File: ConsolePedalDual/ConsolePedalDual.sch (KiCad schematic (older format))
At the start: 14 parts, among them J1 AudioJack3, J2 AudioJack2, J3 Conn_02x25_Odd_Even, J4 Conn_02x25_Odd_Even, SW1 Bypass

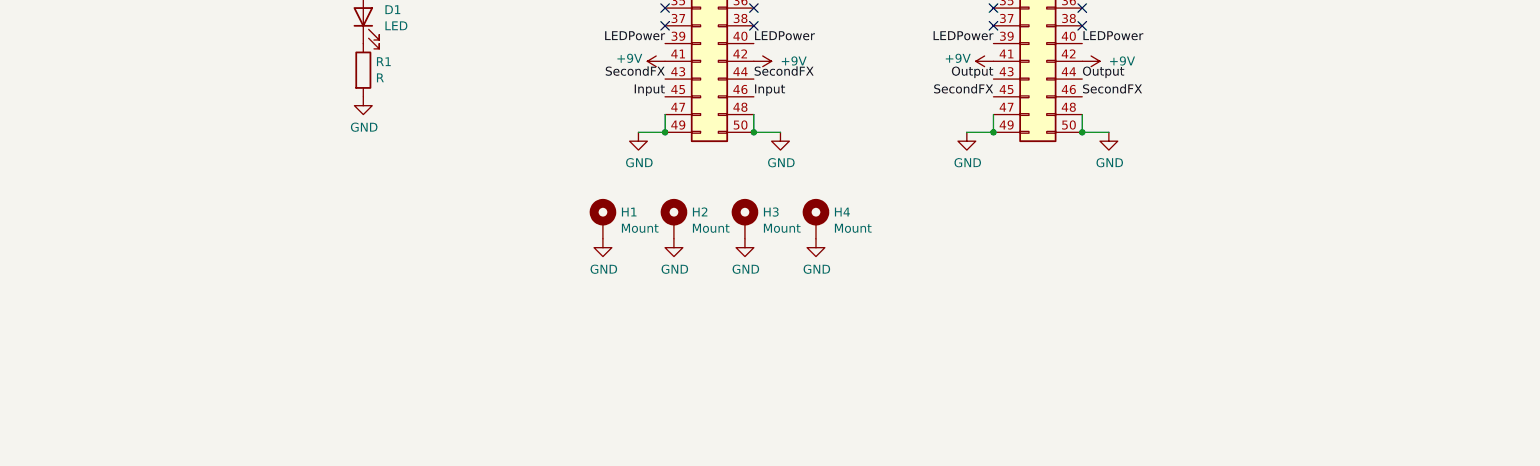
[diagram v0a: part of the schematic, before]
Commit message: Trying to visualize how audio switching ic is going to work
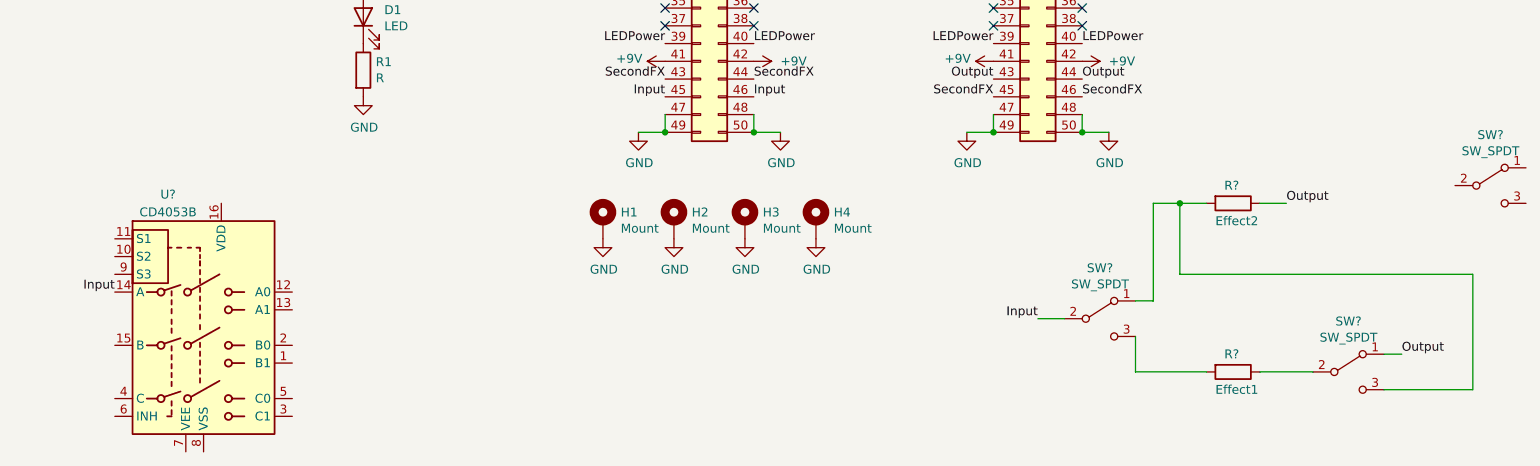
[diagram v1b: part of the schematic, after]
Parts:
- added R?: Effect1, Resistor_THT:R_Axial_DIN0207_L6.3mm_D2.5mm_P10.16mm_Horizontal, symbol Device:R
- added R?: Effect2, Resistor_THT:R_Axial_DIN0207_L6.3mm_D2.5mm_P10.16mm_Horizontal, symbol Device:R
- added SW? (x3): SW_SPDT, symbol Switch:SW_SPDT
- added U?: CD4053B, symbol Analog_Switch:CD4053B
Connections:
- net Input: now also SW?.2 (B), U?.14 (A)
- net Output: now also R?.1, SW?.1 (A)
- new net: R?.2, SW?.1 (A), SW?.3 (C)
- new net: R?.2, SW?.3 (C)
- new net: R?.1, SW?.2 (B)
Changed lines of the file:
@@
 	1    0    0    -1
 $EndComp
+$Comp
+L Analog_Switch:CD4053B U?
+U 1 1 60FF6D67
+P 3200 5700
+F 0 "U?" H 3000 6450 50  0000 C CNN
+F 1 "CD4053B" H 3000 6350 50  0000 C CNN
+F 2 "" H 3350 4950 50  0001 L CNN
+F 3 "http://www.ti.com/lit/ds/symlink/cd4052b.pdf" H 3180 5900 50  0001 C CNN
+	1    3200 5700
+	1    0    0    -1
+$EndComp
+$Comp
+L Switch:SW_SPDT SW?
+U 1 1 60FFC9EC
+P 8250 5650
+F 0 "SW?" H 8250 5935 50  0000 C CNN
+F 1 "SW_SPDT" H 8250 5844 50  0000 C CNN
+F 2 "" H 8250 5650 50  0001 C CNN
+F 3 "~" H 8250 5650 50  0001 C CNN
+	1    8250 5650
+	1    0    0    -1
+$EndComp
+$Comp
+L Switch:SW_SPDT SW?
+U 1 1 60FFD888
+P 10450 4900
+F 0 "SW?" H 10450 5185 50  0000 C CNN
+F 1 "SW_SPDT" H 10450 5094 50  0000 C CNN
+F 2 "" H 10450 4900 50  0001 C CNN
+F 3 "~" H 10450 4900 50  0001 C CNN
+	1    10450 4900
+	1    0    0    -1
+$EndComp
+$Comp
+L Switch:SW_SPDT SW?
+U 1 1 60FFDC32
+P 9650 5950
+F 0 "SW?" H 9650 6235 50  0000 C CNN
+F 1 "SW_SPDT" H 9650 6144 50  0000 C CNN
+F 2 "" H 9650 5950 50  0001 C CNN
+F 3 "~" H 9650 5950 50  0001 C CNN
+	1    9650 5950
+	1    0    0    -1
+$EndComp
+Text Label 7900 5650 2    50   ~ 0
+Input
+Wire Wire Line
+	7900 5650 8050 5650
+Text Label 9950 5850 0    50   ~ 0
+Output
+Wire Wire Line
+	9950 5850 9850 5850
+$Comp
+L Device:R R?
+U 1 1 61005F42
+P 9000 5950
+F 0 "R?" V 8900 5900 50  0000 L CNN
+F 1 "Effect1" V 9100 5850 50  0000 L CNN
+F 2 "Resistor_THT:R_Axial_DIN0207_L6.3mm_D2.5mm_P10.16mm_Horizontal" V 8930 5950 50  0001 C CNN
+F 3 "~" H 9000 5950 50  0001 C CNN
+	1    9000 5950
+	0    1    1    0
+$EndComp
+Wire Wire Line
+	8450 5750 8450 5950
+Wire Wire Line
+	8450 5950 8850 5950
+Wire Wire Line
+	9150 5950 9450 5950
+$Comp
+L Device:R R?
+U 1 1 6100AEB1
+P 9000 5000
+F 0 "R?" V 8900 4950 50  0000 L CNN
+F 1 "Effect2" V 9100 4900 50  0000 L CNN
+F 2 "Resistor_THT:R_Axial_DIN0207_L6.3mm_D2.5mm_P10.16mm_Horizontal" V 8930 5000 50  0001 C CNN
+F 3 "~" H 9000 5000 50  0001 C CNN
+	1    9000 5000
+	0    1    1    0
+$EndComp
+Wire Wire Line
+	8450 5550 8550 5550
+Wire Wire Line
+	8550 5550 8550 5000
+Wire Wire Line
+	8550 5000 8700 5000
+Text Label 9300 5000 0    50   ~ 0
+Output
+Wire Wire Line
+	9300 5000 9150 5000
+Wire Wire Line
+	9850 6050 10350 6050
+Wire Wire Line
+	10350 6050 10350 5400
+Wire Wire Line
+	10350 5400 8700 5400
+Wire Wire Line
+	8700 5400 8700 5000
+Connection ~ 8700 5000
+Wire Wire Line
+	8700 5000 8850 5000
+Text Label 2700 5500 2    50   ~ 0
+Input
 $EndSCHEMATC

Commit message: Minor changes
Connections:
- net +9V: now also U?.16 (VDD)
- net GND: now also U?.6 (INH), U?.7 (VEE), U?.8 (VSS)
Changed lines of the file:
@@
 Text Label 2700 5500 2    50   ~ 0
 Input
+$Comp
+L power:+9V #PWR?
+U 1 1 61013CBC
+P 3300 5000
+F 0 "#PWR?" H 3300 4850 50  0001 C CNN
+F 1 "+9V" H 3200 5150 50  0000 L CNN
+F 2 "" H 3300 5000 50  0001 C CNN
+F 3 "" H 3300 5000 50  0001 C CNN
+	1    3300 5000
+	1    0    0    -1
+$EndComp
+$Comp
+L power:GND #PWR?
+U 1 1 61016125
+P 3100 6450
+F 0 "#PWR?" H 3100 6200 50  0001 C CNN
+F 1 "GND" H 3105 6277 50  0000 C CNN
+F 2 "" H 3100 6450 50  0001 C CNN
+F 3 "" H 3100 6450 50  0001 C CNN
+	1    3100 6450
+	1    0    0    -1
+$EndComp
+Wire Wire Line
+	3200 6400 3100 6400
+Wire Wire Line
+	3100 6400 3100 6450
+Connection ~ 3100 6400
+Wire Wire Line
+	3100 6400 2700 6400
+Wire Wire Line
+	2700 6400 2700 6200
 $EndSCHEMATC

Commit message: Finished schematic. Trying to figure out how to fit all these components on this board
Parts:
- removed R?: Effect1, Resistor_THT:R_Axial_DIN0207_L6.3mm_D2.5mm_P10.16mm_Horizontal, symbol Device:R
- removed R?: Effect2, Resistor_THT:R_Axial_DIN0207_L6.3mm_D2.5mm_P10.16mm_Horizontal, symbol Device:R
- removed SW1: Bypass, Connector_PinSocket_2.54mm:PinSocket_1x02_P2.54mm_Vertical, symbol Switch:SW_SPST
- removed SW? (x3): SW_SPDT, symbol Switch:SW_SPDT
- added C1: 47uF, Capacitor_THT:CP_Radial_D6.3mm_P2.50mm, symbol Device:CP
- added C2, C3, C4, C5, C6, C7: 2.2uF, Capacitor_THT:CP_Radial_D4.0mm_P2.00mm, symbol Device:CP
- added R2, R3: 10K, Resistor_THT:R_Axial_DIN0207_L6.3mm_D2.5mm_P10.16mm_Horizontal, symbol Device:R
- added R4, R5, R6, R7, R8, R9: 510K, Resistor_THT:R_Axial_DIN0207_L6.3mm_D2.5mm_P10.16mm_Horizontal, symbol Device:R
- J3: value Conn_02x25_Odd_Even -> Slot A
- J4: value Conn_02x25_Odd_Even -> Slot B
- R1: value R -> LED
- U1: renamed from U?; footprint (none) -> Package_DIP:DIP-16_W7.62mm_Socket
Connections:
- net +9V: now also R2.1; no longer J3.10 (Pin_10), J3.42 (Pin_42), J4.10 (Pin_10), J4.42 (Pin_42)
- net GND: now also U1.9 (S3), C1.2, R3.2
- net Input: now also C2.2; no longer J3.45 (Pin_45), J3.46 (Pin_46), J3.5 (Pin_5), J3.6 (Pin_6), U1.14 (A)
- net Output: now also C6.2
- net at U1.1 (B1): now also C7.1, R9.1
- net SlotB: now reaches U1.10 (S2)
- net SlotB: now also J4.10 (Pin_10), J4.42 (Pin_42)
- net SlotA: now reaches U1.11 (S1)
- net SlotA: now also J3.10 (Pin_10), J3.42 (Pin_42)
- net at U1.12 (A0): now also C4.1, R6.2
- net at U1.13 (A1): now also C5.1, R7.1
- net at U1.15 (B): now also C3.1, R5.1
- net at U1.2 (B0): now also C6.1, R8.2
- net SecondFX renamed SlotAOutput
- net SlotAOutput: now also C3.2; no longer J4.45 (Pin_45), J4.46 (Pin_46), J4.5 (Pin_5), J4.6 (Pin_6)
- new net: C2.1, R4.1, U1.14 (A)
- new net SlotAInput: C5.2, J3.45 (Pin_45), J3.46 (Pin_46), J3.5 (Pin_5), J3.6 (Pin_6)
- new net SlotBInput: C4.2, C7.2, J4.45 (Pin_45), J4.46 (Pin_46), J4.5 (Pin_5), J4.6 (Pin_6)
- new net VREF: C1.1, R2.2, R3.1, R4.2, R5.2, R6.1, R7.2, R8.1, R9.2
- no-connect marks 53 -> 56
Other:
- moved on the sheet: BT1, D1, D2, H1, H2, H3, H4, J1, J2, J3, J4, R1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

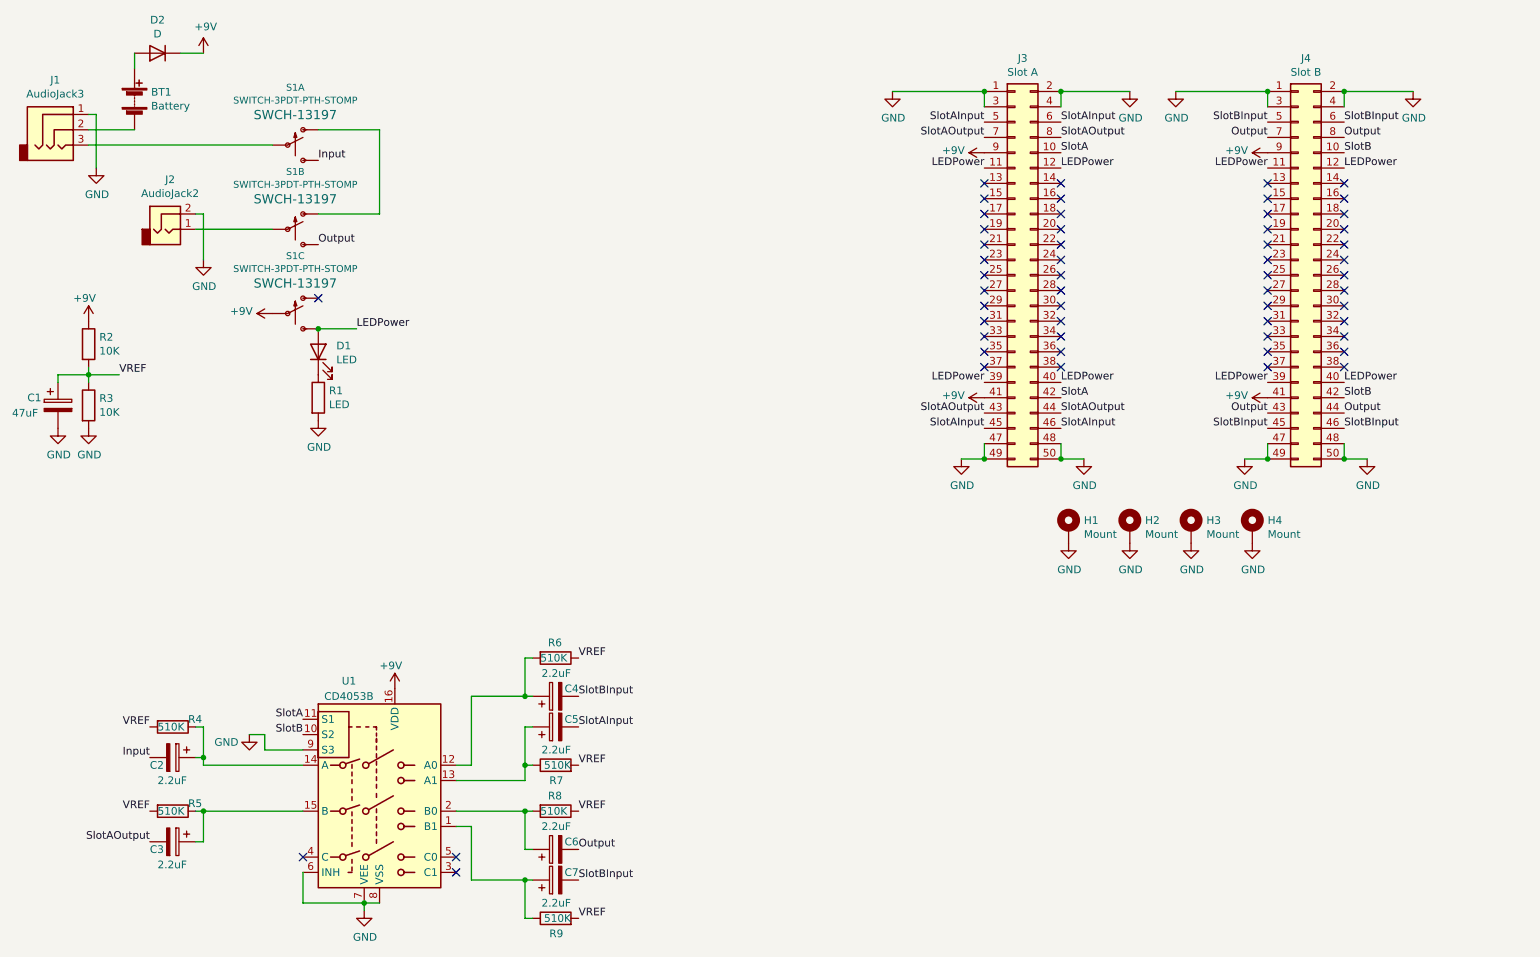
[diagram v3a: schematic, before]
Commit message: Added pull down resistors, fixed mounting hole placements, and fixed 3PDT switch footprint
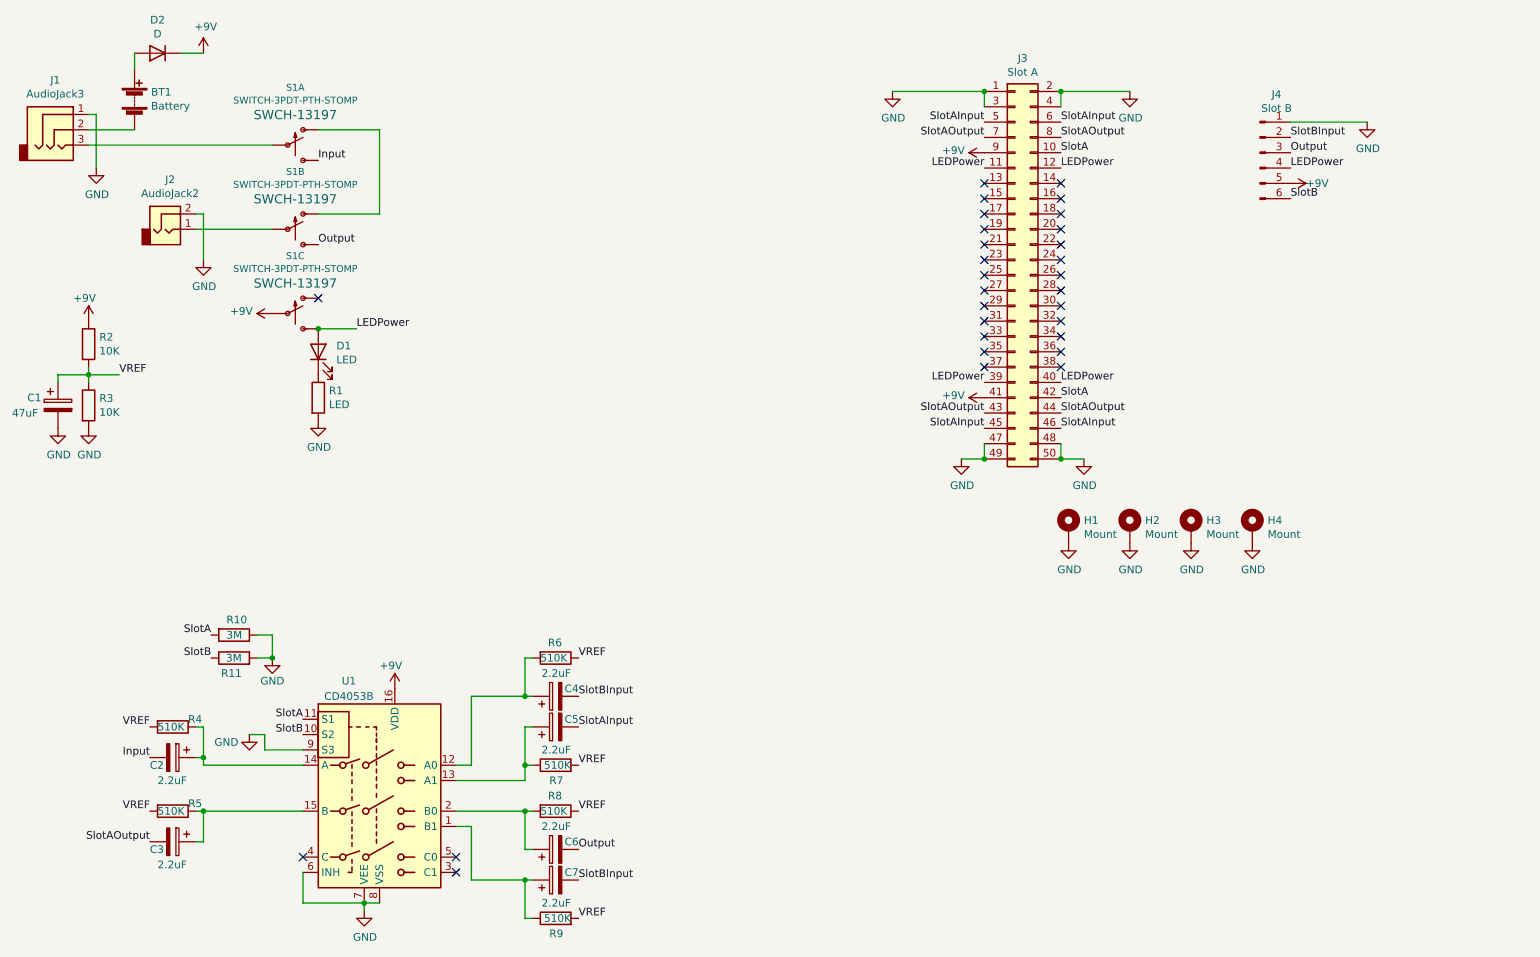
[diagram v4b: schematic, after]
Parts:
- removed J4: Slot B, libraries:n64Socket, symbol Connector_Generic:Conn_02x25_Odd_Even
- added J4: Slot B, Connector_PinSocket_2.54mm:PinSocket_1x06_P2.54mm_Vertical, symbol Connector:Conn_01x06_Male
- added R10, R11: 3M, Resistor_THT:R_Axial_DIN0207_L6.3mm_D2.5mm_P10.16mm_Horizontal, symbol Device:R
- S1: footprint MuffPi:STOMP_SWITCH_3PDT -> libraries:STOMP_SWITCH_3PDT
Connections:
- net +9V: now also J4.5 (Pin_5)
- net GND: now also J4.1 (Pin_1), R10.1, R11.2
- net LEDPower: now also J4.4 (Pin_4)
- net Output: now also J4.3 (Pin_3)
- net SlotA: now also R10.2
- net SlotB: now also J4.6 (Pin_6), R11.1
- net SlotBInput: now also J4.2 (Pin_2)
- no-connect marks 56 -> 30
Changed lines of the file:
@@
 F 0 "S1" H 2600 1976 45  0000 C CNN
 F 1 "SWITCH-3PDT-PTH-STOMP" H 2600 1892 45  0000 C CNN
-F 2 "MuffPi:STOMP_SWITCH_3PDT" H 2650 1850 20  0001 C CNN
+F 2 "libraries:STOMP_SWITCH_3PDT" H 2650 1850 20  0001 C CNN
 F 3 "" H 2650 1600 50  0001 C CNN
 F 4 "SWCH-13197" H 2600 1797 60  0000 C CNN "Field4"
@@
 F 0 "S1" H 2600 2526 45  0000 C CNN
 F 1 "SWITCH-3PDT-PTH-STOMP" H 2600 2442 45  0000 C CNN
-F 2 "MuffPi:STOMP_SWITCH_3PDT" H 2650 2400 20  0001 C CNN
+F 2 "libraries:STOMP_SWITCH_3PDT" H 2650 2400 20  0001 C CNN
 F 3 "" H 2650 2150 50  0001 C CNN
 F 4 "SWCH-13197" H 2600 2347 60  0000 C CNN "Field4"
@@
 F 0 "S1" H 2600 3076 45  0000 C CNN
 F 1 "SWITCH-3PDT-PTH-STOMP" H 2600 2992 45  0000 C CNN
-F 2 "MuffPi:STOMP_SWITCH_3PDT" H 2650 2950 20  0001 C CNN
+F 2 "libraries:STOMP_SWITCH_3PDT" H 2650 2950 20  0001 C CNN
 F 3 "" H 2650 2700 50  0001 C CNN
 F 4 "SWCH-13197" H 2600 2897 60  0000 C CNN "Field4"
@@
 Wire Wire Line
 	2000 1000 1850 1000
-Wire Wire Line
-	8950 1250 8950 1350
-$Comp
-L power:GND #PWR010
-U 1 1 60B0323C
-P 8350 1250
-F 0 "#PWR010" H 8350 1000 50  0001 C CNN
-F 1 "GND" H 8355 1077 50  0000 C CNN
-F 2 "" H 8350 1250 50  0001 C CNN
-F 3 "" H 8350 1250 50  0001 C CNN
-	1    8350 1250
-	1    0    0    -1
-$EndComp
-Wire Wire Line
-	8350 1250 8950 1250
-$Comp
-L power:+9V #PWR012
-U 1 1 60B03245
-P 8950 1650
-F 0 "#PWR012" H 8950 1500 50  0001 C CNN
-F 1 "+9V" V 8965 1778 50  0000 L CNN
-F 2 "" H 8950 1650 50  0001 C CNN
-F 3 "" H 8950 1650 50  0001 C CNN
-	1    8950 1650
-	0    -1   -1   0
-$EndComp
-Text Label 8950 1750 2    50   ~ 0
-LEDPower
-Text Label 9450 3150 0    50   ~ 0
-LEDPower
-Wire Wire Line
-	9450 3550 9450 3650
-Wire Wire Line
-	9450 3650 9600 3650
-$Comp
-L power:GND #PWR016
-U 1 1 60B03257
-P 9600 3650
-F 0 "#PWR016" H 9600 3400 50  0001 C CNN
-F 1 "GND" H 9605 3477 50  0000 C CNN
-F 2 "" H 9600 3650 50  0001 C CNN
-F 3 "" H 9600 3650 50  0001 C CNN
-	1    9600 3650
-	1    0    0    -1
-$EndComp
-$Comp
-L Connector_Generic:Conn_02x25_Odd_Even J4
-U 1 1 60B0325D
-P 9150 2450
-F 0 "J4" H 9200 3867 50  0000 C CNN
-F 1 "Slot B" H 9200 3776 50  0000 C CNN
-F 2 "libraries:n64Socket" H 9150 2450 50  0001 C CNN
-F 3 "~" H 9150 2450 50  0001 C CNN
-	1    9150 2450
-	1    0    0    -1
-$EndComp
-Connection ~ 8950 1250
-Connection ~ 9450 3650
-Wire Wire Line
-	9450 1350 9450 1250
-$Comp
-L power:GND #PWR017
-U 1 1 60B03266
-P 9900 1250
-F 0 "#PWR017" H 9900 1000 50  0001 C CNN
-F 1 "GND" H 9905 1077 50  0000 C CNN
-F 2 "" H 9900 1250 50  0001 C CNN
-F 3 "" H 9900 1250 50  0001 C CNN
-	1    9900 1250
-	1    0    0    -1
-$EndComp
-Wire Wire Line
-	9450 1250 9900 1250
-Connection ~ 9450 1250
-Text Label 9450 1750 0    50   ~ 0
-LEDPower
-Text Label 8950 3150 2    50   ~ 0
-LEDPower
-$Comp
-L power:+9V #PWR013
-U 1 1 60B03278
-P 8950 3250
-F 0 "#PWR013" H 8950 3100 50  0001 C CNN
-F 1 "+9V" V 8965 3378 50  0000 L CNN
-F 2 "" H 8950 3250 50  0001 C CNN
-F 3 "" H 8950 3250 50  0001 C CNN
-	1    8950 3250
-	0    -1   -1   0
-$EndComp
-Wire Wire Line
-	8950 3550 8950 3650
-$Comp
-L power:GND #PWR011
-U 1 1 60B03281
-P 8800 3650
-F 0 "#PWR011" H 8800 3400 50  0001 C CNN
-F 1 "GND" H 8805 3477 50  0000 C CNN
-F 2 "" H 8800 3650 50  0001 C CNN
-F 3 "" H 8800 3650 50  0001 C CNN
-	1    8800 3650
-	1    0    0    -1
-$EndComp
-Wire Wire Line
-	8800 3650 8950 3650
-Connection ~ 8950 3650
-NoConn ~ 9450 1850
-NoConn ~ 9450 1950
-NoConn ~ 9450 2050
-NoConn ~ 9450 2150
-NoConn ~ 9450 2250
-NoConn ~ 9450 2350
-NoConn ~ 9450 2450
-NoConn ~ 9450 2550
-NoConn ~ 9450 2650
-NoConn ~ 9450 2750
-NoConn ~ 9450 2850
-NoConn ~ 9450 2950
-NoConn ~ 9450 3050
-NoConn ~ 8950 3050
-NoConn ~ 8950 2950
-NoConn ~ 8950 2850
-NoConn ~ 8950 2750
-NoConn ~ 8950 2650
-NoConn ~ 8950 2550
-NoConn ~ 8950 2450
-NoConn ~ 8950 2350
-NoConn ~ 8950 2250
-NoConn ~ 8950 2150
-NoConn ~ 8950 2050
-NoConn ~ 8950 1950
-NoConn ~ 8950 1850
 $Comp
 L Mechanical:MountingHole_Pad H1
@@
 Text Label 7600 1650 0    50   ~ 0
 SlotA
-Text Label 9450 1650 0    50   ~ 0
-SlotB
 Text Label 7600 3250 0    50   ~ 0
 SlotA
-Text Label 9450 3250 0    50   ~ 0
-SlotB
 Text Label 7600 1450 0    50   ~ 0
 SlotAInput
@@
 Text Label 7600 3350 0    50   ~ 0
 SlotAOutput
-Text Label 8950 1450 2    50   ~ 0
-SlotBInput
-Text Label 9450 1450 0    50   ~ 0
-SlotBInput
-Text Label 8950 3450 2    50   ~ 0
-SlotBInput
-Text Label 9450 3450 0    50   ~ 0
-SlotBInput
 Text Label 4450 6200 0    50   ~ 0
 Output
 Text Label 4450 5400 0    50   ~ 0
 SlotAInput
-Text Label 9450 3350 0    50   ~ 0
-Output
-Text Label 8950 3350 2    50   ~ 0
-Output
-Text Label 9450 1550 0    50   ~ 0
-Output
-Text Label 8950 1550 2    50   ~ 0
-Output
 NoConn ~ 2650 6250
 $Comp
@@
 	3750 5200 4100 5200
 Connection ~ 4100 5200
+Text Label 2050 4800 2    50   ~ 0
+SlotA
+Text Label 2050 4950 2    50   ~ 0
+SlotB
+$Comp
+L Device:R R10
+U 1 1 61456261
+P 2200 4800
+F 0 "R10" V 2100 4750 50  0000 L CNN
+F 1 "3M" V 2200 4750 50  0000 L CNN
+F 2 "Resistor_THT:R_Axial_DIN0207_L6.3mm_D2.5mm_P10.16mm_Horizontal" V 2130 4800 50  0001 C CNN
+F 3 "~" H 2200 4800 50  0001 C CNN
+	1    2200 4800
+	0    1    1    0
+$EndComp
+$Comp
+L power:GND #PWR025
+U 1 1 61457C6D
+P 2450 4950
+F 0 "#PWR025" H 2450 4700 50  0001 C CNN
+F 1 "GND" H 2450 4800 50  0000 C CNN
+F 2 "" H 2450 4950 50  0001 C CNN
+F 3 "" H 2450 4950 50  0001 C CNN
+	1    2450 4950
+	1    0    0    -1
+$EndComp
+Wire Wire Line
+	2450 4800 2350 4800
+Wire Wire Line
+	2350 4950 2450 4950
+Wire Wire Line
+	2450 4800 2450 4950
+Connection ~ 2450 4950
+$Comp
+L Device:R R11
+U 1 1 61456971
+P 2200 4950
+F 0 "R11" V 2100 4900 50  0000 L CNN
+F 1 "3M" V 2200 4900 50  0000 L CNN
+F 2 "Resistor_THT:R_Axial_DIN0207_L6.3mm_D2.5mm_P10.16mm_Horizontal" V 2130 4950 50  0001 C CNN
+F 3 "~" H 2200 4950 50  0001 C CNN
+	1    2200 4950
+	0    -1   -1   0
+$EndComp
+$Comp
+L Connector:Conn_01x06_Male J4
+U 1 1 61463F82
+P 8900 1650
+F 0 "J4" H 9008 2031 50  0000 C CNN
+F 1 "Slot B" H 9008 1940 50  0000 C CNN
+F 2 "Connector_PinSocket_2.54mm:PinSocket_1x06_P2.54mm_Vertical" H 8900 1650 50  0001 C CNN
+F 3 "~" H 8900 1650 50  0001 C CNN
+	1    8900 1650
+	1    0    0    -1
+$EndComp
+$Comp
+L power:GND #PWR011
+U 1 1 6146637B
+P 9600 1450
+F 0 "#PWR011" H 9600 1200 50  0001 C CNN
+F 1 "GND" H 9605 1277 50  0000 C CNN
+F 2 "" H 9600 1450 50  0001 C CNN
+F 3 "" H 9600 1450 50  0001 C CNN
+	1    9600 1450
+	1    0    0    -1
+$EndComp
+Text Label 9100 1550 0    50   ~ 0
+SlotBInput
+Wire Wire Line
+	9100 1450 9600 1450
+Text Label 9100 1650 0    50   ~ 0
+Output
+Text Label 9100 1950 0    50   ~ 0
+SlotB
+$Comp
+L power:+9V #PWR010
+U 1 1 6146F26B
+P 9100 1850
+F 0 "#PWR010" H 9100 1700 50  0001 C CNN
+F 1 "+9V" V 9100 1950 50  0000 L CNN
+F 2 "" H 9100 1850 50  0001 C CNN
+F 3 "" H 9100 1850 50  0001 C CNN
+	1    9100 1850
+	0    1    1    0
+$EndComp
+Text Label 9100 1750 0    50   ~ 0
+LEDPower
 $EndSCHEMATC
